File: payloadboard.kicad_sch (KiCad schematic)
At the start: 14 parts, among them J1 TFM-110-12-L-D-A, J2 FLE-105-01-G-DV-A, J3 Micro_SD_Card, Q4 MMBT2907

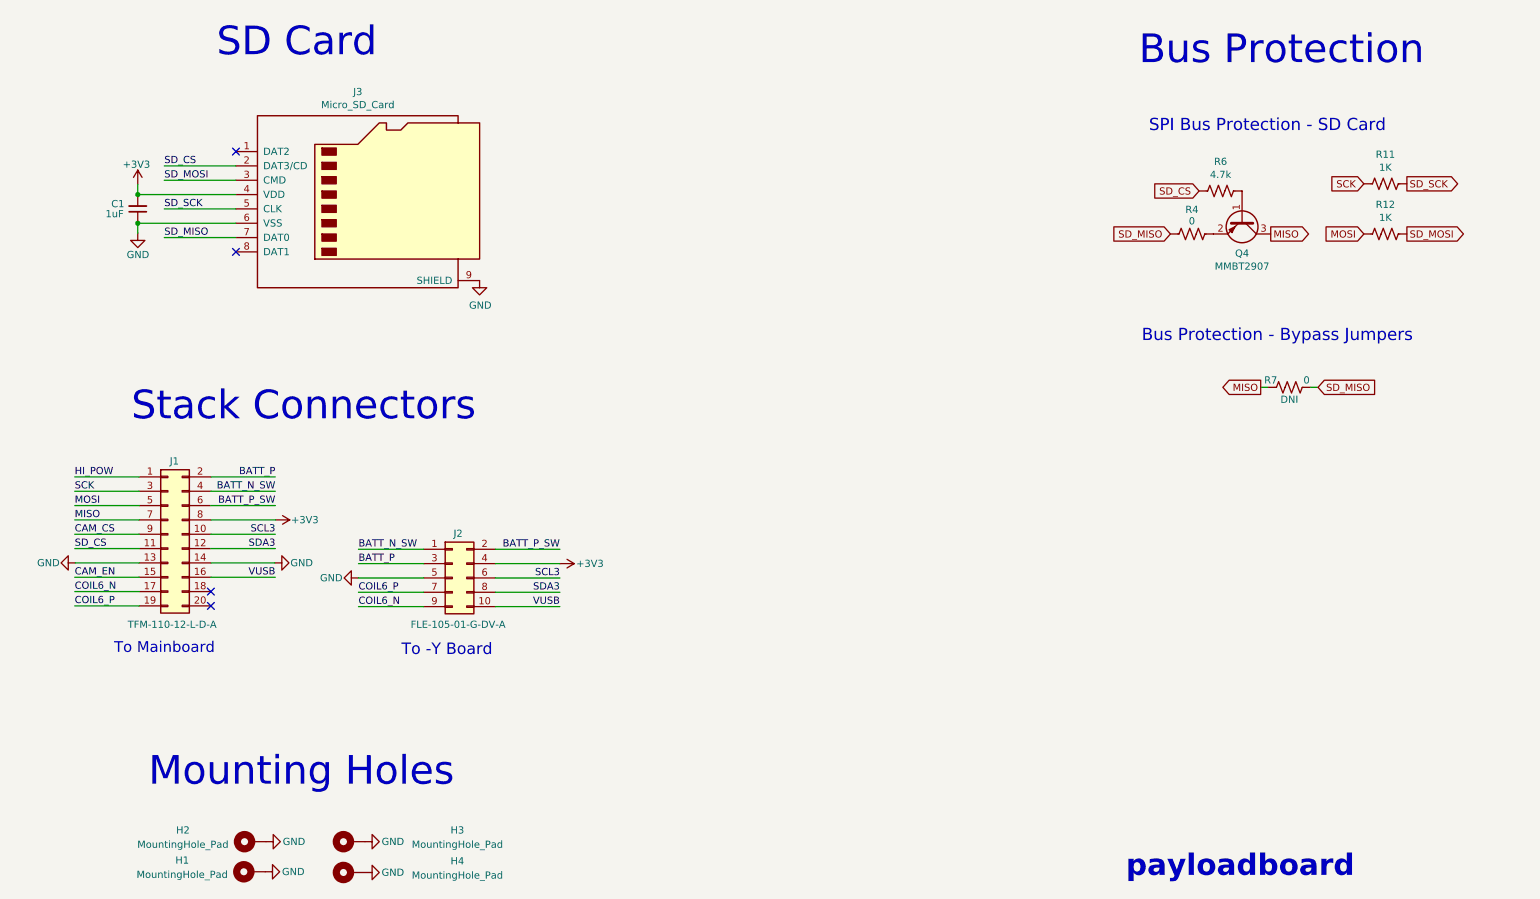
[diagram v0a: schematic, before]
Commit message: Added 3.3V power regulator with enable pin and new stack connector
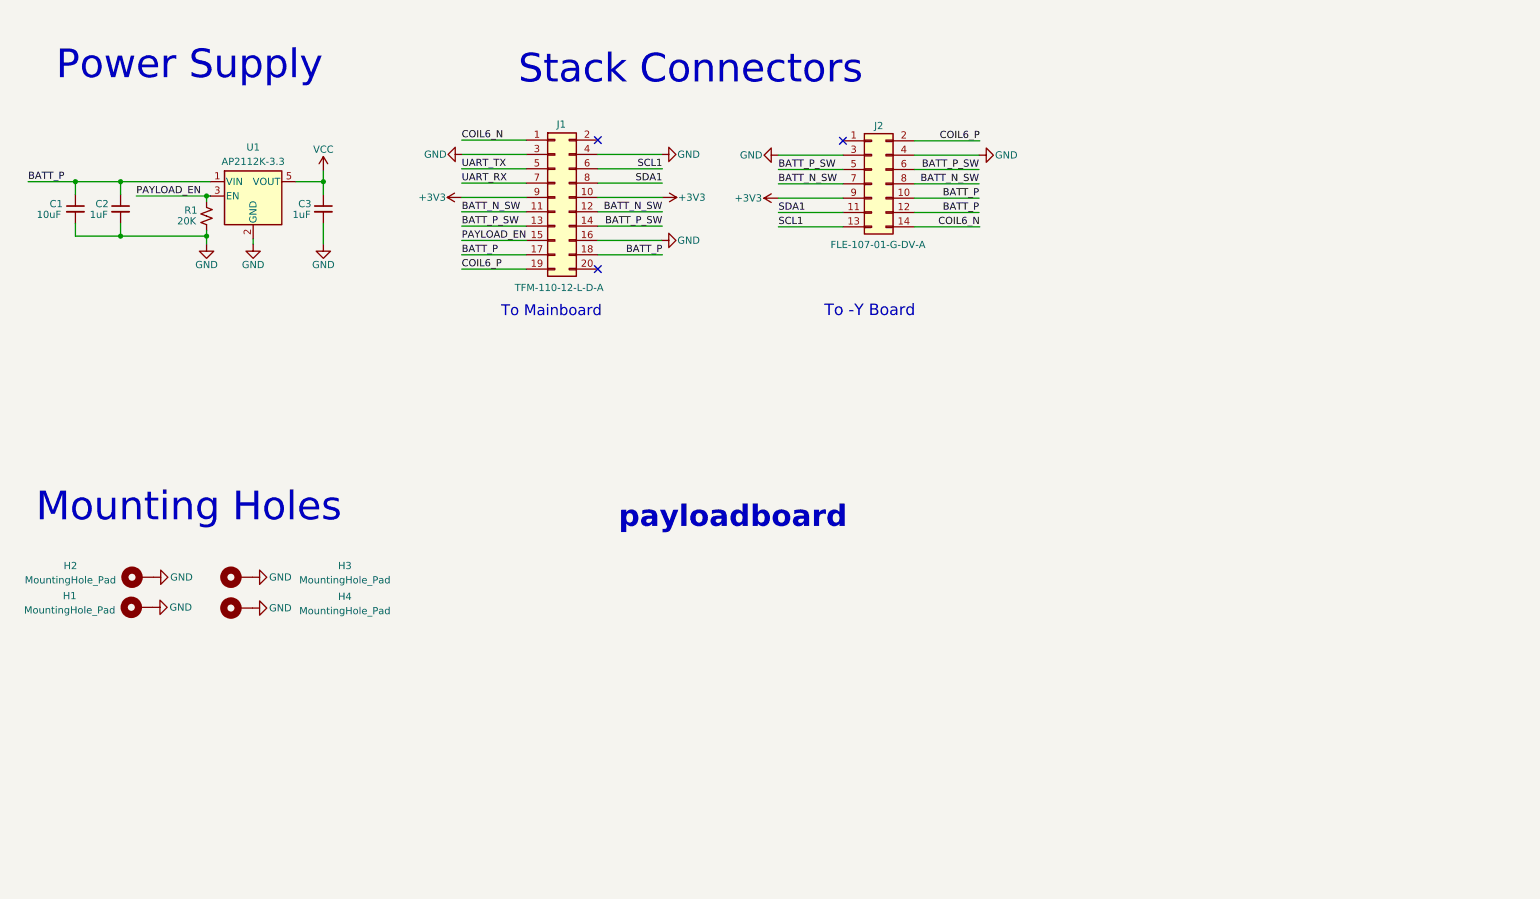
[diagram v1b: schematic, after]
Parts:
- removed J2: FLE-105-01-G-DV-A, cameraboard:SAMTEC_FLE-105-01-G-DV-A, symbol Connector_Generic:Conn_02x05_Odd_Even
- removed J3: Micro_SD_Card, cameraboard:MOLEX_503398-1892, symbol Connector:Micro_SD_Card
- removed Q4: MMBT2907, Package_TO_SOT_SMD:SOT-23, symbol mainboard:MMBT2907
- removed R11, R12: 1K, Resistor_SMD:R_0603_1608Metric, symbol Device:R_US
- removed R4, R7: 0, Resistor_SMD:R_0603_1608Metric, symbol Device:R_US
- removed R6: 4.7k, Resistor_SMD:R_0603_1608Metric, symbol Device:R_US
- added C2, C3: 1uF, Capacitor_SMD:C_0805_2012Metric, symbol Device:C_Small
- added J2: FLE-107-01-G-DV-A, cameraboard:SAMTEC_FLE-107-01-G-DV-A, symbol Connector_Generic:Conn_02x07_Odd_Even
- added R1: 20K, Resistor_SMD:R_0805_2012Metric, symbol Device:R_Small_US
- added U1: AP2112K-3.3, Package_TO_SOT_SMD:SOT-23-5, symbol Regulator_Linear:AP2112K-3.3
- C1: value 1uF -> 10uF; footprint Capacitor_SMD:C_0603_1608Metric_Pad1.08x0.95mm_HandSolder -> Capacitor_SMD:C_0805_2012Metric
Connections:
- net CAM_CS is gone; now on net +3V3: J1.9 (Pin_9)
- net HI_POW is gone; now on net COIL6_N: J1.1 (Pin_1)
- net SCK is gone; now on net GND: J1.3 (Pin_3)
- net SCL3 is gone; now on net +3V3: J1.10 (Pin_10)
- net SDA3 is gone; now on net BATT_N_SW: J1.12 (Pin_12)
- net SD_CS is gone; now on net BATT_N_SW: J1.11 (Pin_11)
- net VUSB is gone; now on net GND: J1.16 (Pin_16)
- net +3V3: now also J2.9 (Pin_9); no longer C1.2, J1.8 (Pin_8)
- net BATT_N_SW: now also J2.7 (Pin_7), J2.8 (Pin_8); no longer J1.4 (Pin_4)
- net BATT_P: now also C1.1, J1.17 (Pin_17), J1.18 (Pin_18), C2.1, J2.10 (Pin_10), J2.12 (Pin_12), U1.1 (VIN); no longer J1.2 (Pin_2)
- net BATT_P_SW: now also J1.13 (Pin_13), J1.14 (Pin_14), J2.5 (Pin_5), J2.6 (Pin_6); no longer J1.6 (Pin_6)
- net COIL6_N: now also J2.14 (Pin_14); no longer J1.17 (Pin_17)
- net COIL6_P: now also J2.2 (Pin_2)
- net GND: now also C1.2, J1.4 (Pin_4), C2.2, C3.2, J2.3 (Pin_3), J2.4 (Pin_4), R1.2, U1.2 (GND); no longer C1.1, J1.13 (Pin_13), J1.14 (Pin_14)
- net CAM_EN renamed PAYLOAD_EN
- net PAYLOAD_EN: now also R1.1, U1.3 (EN)
- net MISO renamed UART_RX
- net MOSI renamed UART_TX
- new net SCL1: J1.6 (Pin_6), J2.13 (Pin_13)
- new net SDA1: J1.8 (Pin_8), J2.11 (Pin_11)
- new net VCC: C3.1, U1.5 (VOUT)
- no-connect marks 4 -> 3
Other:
- note added: "Power Supply"
- note removed: "Bus Protection"
- note removed: "Bus Protection - Bypass Jumpers"
- note removed: "SD Card"
- note removed: "SPI Bus Protection - SD Card"
- moved on the sheet: H1, H2, H3, H4, J1
